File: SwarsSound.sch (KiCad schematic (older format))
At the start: 9 parts, among them P1 Main_Connector

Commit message: Add files via upload
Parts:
- added 5F/H, F/H-5: 74LS125, symbol 74xx:74LS125
- added C1, C12, C61, C8, C9: 0.1uf, symbol Device:C
- added H-5: LS74, symbol Star_Wars_Vector_PCB:LS74
- added R1: 1000, symbol Device:R_US
- added R2, R3: 10K, symbol Device:R_US
- F_5: symbol Star_Wars_Audio_PCB:LS161A -> SwarsSound-rescue:LS161A-Star_Wars_Audio_PCB
- gave numbers to parts that had none: 3
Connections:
- net labels added: MAINFLAG, P, SA0, SA1, SA10, SA11, SA12, SA13, SA14, SA2, SA3, SA4, SA5, SA6, SA7, SA8, SA9, SD0, SD1, SD2, SD3, SD4, SD5, SD6, SD7, SOUNDFLAG, SR\~W, S~IRQ, ~SOUNDREAD, ~SOUNDWR, ~SRES, ɸE
- wire segments 143 -> 197
- no-connect marks 43 -> 51
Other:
- note added: "Microprocessor"
- note added: "Parallel Interface with Full Handshaking"
- moved on the sheet: C6, H_2E, J_3B, J_5, K-3, K_5, R4

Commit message: Add files via upload
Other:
- note added: "Interface Flag Reader"
- moved on the sheet: 5F/HB, 5F/HC
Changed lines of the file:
@@
 L 74xx:74LS125 5F/H
 U 3 1 60E16230
-P 13400 8250
-F 0 "5F/H" H 13400 8567 50  0000 C CNN
-F 1 "74LS125" H 13400 8476 50  0000 C CNN
-F 2 "" H 13400 8250 50  0001 C CNN
-F 3 "http://www.ti.com/lit/gpn/sn74LS125" H 13400 8250 50  0001 C CNN
-	3    13400 8250
+P 13675 8400
+F 0 "5F/H" H 13675 8717 50  0000 C CNN
+F 1 "74LS125" H 13675 8626 50  0000 C CNN
+F 2 "" H 13675 8400 50  0001 C CNN
+F 3 "http://www.ti.com/lit/gpn/sn74LS125" H 13675 8400 50  0001 C CNN
+	3    13675 8400
 	1    0    0    -1
 $EndComp
@@
 L 74xx:74LS125 5F/H
 U 2 1 60E1786D
-P 13400 9150
-F 0 "5F/H" H 13400 9467 50  0000 C CNN
-F 1 "74LS125" H 13400 9376 50  0000 C CNN
-F 2 "" H 13400 9150 50  0001 C CNN
-F 3 "http://www.ti.com/lit/gpn/sn74LS125" H 13400 9150 50  0001 C CNN
-	2    13400 9150
+P 13675 9300
+F 0 "5F/H" H 13675 9617 50  0000 C CNN
+F 1 "74LS125" H 13675 9526 50  0000 C CNN
+F 2 "" H 13675 9300 50  0001 C CNN
+F 3 "http://www.ti.com/lit/gpn/sn74LS125" H 13675 9300 50  0001 C CNN
+	2    13675 9300
 	1    0    0    -1
 $EndComp
-Text GLabel 13100 8250 0    60   Input ~ 0
+Text GLabel 13375 8400 0    60   Input ~ 0
 MAINFLAG
-Text GLabel 13100 9150 0    60   Input ~ 0
+Text GLabel 13375 9300 0    60   Input ~ 0
 SOUNDFLAG
 Wire Wire Line
-	13350 9150 13100 9150
-Text GLabel 13700 8250 2    60   Input ~ 0
+	13625 9300 13375 9300
+Text GLabel 13975 8400 2    60   Input ~ 0
 PD7
 Wire Wire Line
-	13400 8500 13400 8650
+	13675 8650 13675 8800
 Wire Wire Line
-	13400 8650 12375 8650
-Text GLabel 12150 8650 0    60   Input ~ 0
+	13675 8800 12650 8800
+Text GLabel 12425 8800 0    60   Input ~ 0
 ~FLAGREAD
 Wire Wire Line
-	12375 8650 12375 9625
+	12650 8800 12650 9775
 Wire Wire Line
-	12375 9625 13400 9625
+	12650 9775 13675 9775
 Wire Wire Line
-	13400 9625 13400 9400
-Connection ~ 12375 8650
+	13675 9775 13675 9550
+Connection ~ 12650 8800
 Wire Wire Line
-	12375 8650 12150 8650
-Text GLabel 13700 9150 2    60   Input ~ 0
+	12650 8800 12425 8800
+Text GLabel 13975 9300 2    60   Input ~ 0
 PD6
 Wire Notes Line width 40 style solid rgb(0, 0, 0)
@@
 Wire Notes Line width 40 style solid rgb(0, 0, 0)
 	11225 9975 11225 7500
+Text Notes 14000 7775 2    100  ~ 20
+Interface Flag Reader
 $EndSCHEMATC

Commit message: Joint session
Added footprints and plopped chips on nonexistent board.
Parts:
- removed 5F/H: 74LS125, symbol 74xx:74LS125
- removed F_5: LS161A, symbol SwarsSound-rescue:LS161A-Star_Wars_Audio_PCB
- added A-3: NE556, Star_Wars_Vector_PCB:DIP14, symbol SwarsSound-rescue:NE556-Timer
- added B-2, C-3, C-4: TL084, Star_Wars_Vector_PCB:DIP14, symbol SwarsSound-rescue:TL084-Amplifier_Operational
- added B-3: RD5106A, Star_Wars_Vector_PCB:DIP8, symbol SwarsSound-rescue:RD5106A-Audio
- added C/D-1: TMS-5220, Star_Wars_Main_PCB:DIP28, symbol Star_Wars_Audio_PCB:TMS-5220
- added C10, C11, C16, C17, C18, C19, C2, C20, C28, C3, C4, C5, C7: 0.1uf, Star_Wars_Vector_PCB:GenericComp, symbol Device:C
- added C22, C23, C24, C25, C26, C27, C30, C31, C32, C34, C36, C37, C38, C40, C41, C42, C43, C45, C54, C55, C59, C60: 0.1, Star_Wars_Vector_PCB:GenericComp, symbol Device:C
- added C29, C33, C35, C39: 1000pf, Star_Wars_Vector_PCB:GenericComp, symbol Device:C
- added C44: 0.01, Star_Wars_Vector_PCB:GenericComp, symbol Device:C
- added C46, C48, C49, C50, C56, C57, C58: .0027, Star_Wars_Vector_PCB:GenericComp, symbol Device:C
- added C47, C53: 100, Star_Wars_Vector_PCB:GenericComp, symbol Device:C
- added C51: 0.47, Star_Wars_Vector_PCB:GenericComp, symbol Device:C
- added C52: 10, Star_Wars_Vector_PCB:GenericComp, symbol Device:C
- added D-2: CI/O 3, Package_DIP:DIP-40_W15.24mm, symbol SwarsSound-rescue:POKEY-Star_Wars_Audio_PCB
- added D-3: CI/O 2, Package_DIP:DIP-40_W15.24mm, symbol SwarsSound-rescue:POKEY-Star_Wars_Audio_PCB
- added D-4: CI/O 1, Package_DIP:DIP-40_W15.24mm, symbol SwarsSound-rescue:POKEY-Star_Wars_Audio_PCB
- added D-5: CI/O 0, Package_DIP:DIP-40_W15.24mm, symbol SwarsSound-rescue:POKEY-Star_Wars_Audio_PCB
- added E-1: 6532A PIA, Package_DIP:DIP-40_W15.24mm, symbol SwarsSound-rescue:6532A-Star_Wars_Audio_PCB
- added F-2: CD4069/74C04, Star_Wars_Vector_PCB:DIP14, symbol SwarsSound-rescue:4069-4xxx
- added F-3, F-5: LS161A, Star_Wars_Vector_PCB:DIP16, symbol Star_Wars_Audio_PCB:LS161A
- added F/H-1: 6116-2K-RAM, Star_Wars_Vector_PCB:DDIP24, symbol SwarsSound-rescue:6116-2K-RAM
- added unit 3 of F/H-5
- added unit 2 of F/H-5
- added H-1, J/K-1: 2764, Star_Wars_Main_PCB:DIP28, symbol star_wars_arcade_main_pcb:2764
- added H-2: LS04, Star_Wars_Vector_PCB:DIP14, symbol Star_Wars_Vector_PCB:LS04
- added H-3: LS00, Star_Wars_Vector_PCB:DIP14, symbol Asteroids:LS00
- added J-2: LS139, Star_Wars_Vector_PCB:DIP16, symbol Asteroids:LS139
- added unit 1 of J-3
- added P2: aud_con, Star_Wars_Vector_PCB:Aud_Con_7, symbol Star_Wars_Audio_PCB:aud_con
- added P3: edge_con, Star_Wars_Vector_PCB:J20, symbol Star_Wars_Audio_PCB:edge_con
- added Q1, Q2: 2N3906f, Star_Wars_Vector_PCB:GenericTrans, symbol SwarsSound-rescue:2N3906f-Transistor_BJT
- added Q3, Q4: 2N3904, Package_TO_SOT_THT:TO-92_Inline, symbol Transistor_BJT:2N3904
- added R10, R13, R17, R37, R5, R6: 10K, Star_Wars_Vector_PCB:GenericComp, symbol Device:R_US
- added R11, R14, R16: 3300, Star_Wars_Vector_PCB:GenericComp, symbol Device:R_US
- added R12, R15, R20, R22, R24, R26, R28: 1000, Star_Wars_Vector_PCB:GenericComp, symbol Device:R_US
- added R18: 1800, Star_Wars_Vector_PCB:GenericComp, symbol Device:R_US
- added R19: 100K, Star_Wars_Vector_PCB:GenericComp, symbol Device:R_US
- added R21, R23, R50, R54, R55: 47K, Star_Wars_Vector_PCB:GenericComp, symbol Device:R_US
- added R25, R27: 82K, Star_Wars_Vector_PCB:GenericComp, symbol Device:R_US
- added R29: 15K, Star_Wars_Vector_PCB:GenericComp, symbol Device:R_US
- added R30, R39, R40, R42, R46, R47: 12K, Star_Wars_Vector_PCB:GenericComp, symbol Device:R_US
- added R31, R32: 560K, Star_Wars_Vector_PCB:GenericComp, symbol Device:R_US
- added R33, R34: 4700, Star_Wars_Vector_PCB:GenericComp, symbol Device:R_US
- added R35, R51, R56: 2.2K, Star_Wars_Vector_PCB:GenericComp, symbol Device:R_US
- added R36: 15, Star_Wars_Vector_PCB:GenericComp, symbol Device:R_US
- added R38: 470, Star_Wars_Vector_PCB:GenericComp, symbol Device:R_US
- added R41: 68K, Star_Wars_Vector_PCB:GenericComp, symbol Device:R_US
- added R43: 1500, Star_Wars_Vector_PCB:GenericComp, symbol Device:R_US
- added R44, R8, R9: 100, Star_Wars_Vector_PCB:GenericComp, symbol Device:R_US
- added R45: 470K, Star_Wars_Vector_PCB:GenericComp, symbol Device:R_US
- added R48, R49, R52, R53: 22K, Star_Wars_Vector_PCB:GenericComp, symbol Device:R_US
- added TP1, TP10, TP2, TP7, TP8, TP9: TP, Star_Wars_Vector_PCB:TEST_POINT, symbol Star_Wars_Vector_PCB:TP
- C1, C12, C6, C61, C8, C9, R1, R2, R3, R4: footprint (none) -> Star_Wars_Vector_PCB:GenericComp
- F/H-5, H-5, H_2: footprint (none) -> Star_Wars_Vector_PCB:DIP14
- J-3: renamed from J_3; footprint (none) -> Star_Wars_Vector_PCB:DIP16
- J-5: renamed from J_5; footprint (none) -> Star_Wars_Vector_PCB:DIP20
- K-3: footprint (none) -> Star_Wars_Vector_PCB:DDIP40
- K-5: renamed from K_5; footprint (none) -> Star_Wars_Vector_PCB:DIP20
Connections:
- net labels added: +12V, +5A, -5V, AUD, CO0, CO1, CO2, CO3, DRCV, DXMT, LT_AUD, PA0, PA1, PA2, PA3, PA5, PB0, PB1, PB2, PB3, PB4, PB5, PB6, PB7, RCK, RT_AUD, SPEECH, SUM, ~CI\O, ~CI\O0, ~CI\O1, ~CI\O2, ~CI\O3, ~PIA, ~SRAM, ~SROM0, ~SROM1
- wire segments 197 -> 497
- no-connect marks 51 -> 101
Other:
- note added: "Address Decoders"
- note added: "Buffers"
- note added: "Delay"
- note added: "Delay Clock"
- note added: "Filter"
- note added: "Music and Sound Effects Generators"
- note added: "Not fitted"
- note added: "Output and Summing Amplifiers"
- note added: "Peripheral Interface Adapter"
- note added: "SELF-TEST"
- note added: "Sound RAM\n"
- note added: "Sound ROM"
- note added: "Speech Synthesizer"
- note added: "Speech Synthesizer Clock Generator"
- note added: "Speech Synthesizer Power Switch"
- note added: "Summing Amplifier"
- note added: "Used by buffers"
- moved on the sheet: C1, C6, C8, C9, F/H-5E, H-5B, J-3B, J-5, K-5

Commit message: Began board layout
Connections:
- net +12V: now also A-3.14 (VCC)
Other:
- moved on the sheet: C45
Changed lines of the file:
@@
 $EndComp
 NoConn ~ 22575 14550
-Wire Wire Line
-	22375 14150 22225 14150
-Wire Wire Line
-	22225 13925 22225 14100
 $Comp
 L power:GND #PWR0130
 U 1 1 61A178FF
-P 22675 14150
-F 0 "#PWR0130" H 22675 13900 50  0001 C CNN
-F 1 "GND" H 22680 13977 50  0000 C CNN
-F 2 "" H 22675 14150 50  0001 C CNN
-F 3 "" H 22675 14150 50  0001 C CNN
-	1    22675 14150
+P 22775 14100
+F 0 "#PWR0130" H 22775 13850 50  0001 C CNN
+F 1 "GND" H 22780 13927 50  0000 C CNN
+F 2 "" H 22775 14100 50  0001 C CNN
+F 3 "" H 22775 14100 50  0001 C CNN
+	1    22775 14100
 	1    0    0    -1
 $EndComp
-Connection ~ 22225 14100
 $Comp
 L Device:C C45
 U 1 1 619FBD8D
-P 22525 14150
-F 0 "C45" V 22725 14150 50  0000 C CNN
-F 1 "0.1" V 22650 14150 50  0000 C CNN
-F 2 "Star_Wars_Vector_PCB:GenericComp" H 22563 14000 50  0001 C CNN
-F 3 "~" H 22525 14150 50  0001 C CNN
-	1    22525 14150
+P 22625 14100
+F 0 "C45" V 22825 14100 50  0000 C CNN
+F 1 "0.1" V 22750 14100 50  0000 C CNN
+F 2 "Star_Wars_Vector_PCB:GenericComp" H 22663 13950 50  0001 C CNN
+F 3 "~" H 22625 14100 50  0001 C CNN
+	1    22625 14100
 	0    -1   -1   0
 $EndComp
 Connection ~ 21925 14100
 Wire Wire Line
-	22225 14100 22225 14150
-Wire Wire Line
-	21925 14100 22225 14100
+	21925 14100 22250 14100
 Wire Wire Line
 	21925 14100 21925 14150
 Wire Wire Line
 	21050 14100 21925 14100
-Connection ~ 21575 14700
 Wire Wire Line
 	21575 14550 21575 14700
@@
 	1    0    0    -1
 $EndComp
-$Comp
-L SwarsSound-rescue:NE556-Timer A-3
-U 1 1 618D148D
-P 22075 14550
-F 0 "A-3" H 22125 14600 50  0000 R CNN
-F 1 "NE556" H 22150 14500 50  0000 R CNN
-F 2 "Star_Wars_Vector_PCB:DIP14" H 22075 14550 50  0001 C CNN
-F 3 "http://www.ti.com/lit/ds/symlink/ne556.pdf" H 22075 14550 50  0001 C CNN
-	1    22075 14550
-	1    0    0    -1
-$EndComp
 Wire Wire Line
 	22450 15425 22450 15250
@@
 L power:+12V #PWR0236
 U 1 1 61EDFE84
-P 22225 13925
-F 0 "#PWR0236" H 22225 13775 50  0001 C CNN
-F 1 "+12V" H 22240 14098 50  0000 C CNN
-F 2 "" H 22225 13925 50  0001 C CNN
-F 3 "" H 22225 13925 50  0001 C CNN
-	1    22225 13925
+P 22250 13925
+F 0 "#PWR0236" H 22250 13775 50  0001 C CNN
+F 1 "+12V" H 22265 14098 50  0000 C CNN
+F 2 "" H 22250 13925 50  0001 C CNN
+F 3 "" H 22250 13925 50  0001 C CNN
+	1    22250 13925
 	1    0    0    -1
 $EndComp
@@
 	1    0    0    -1
 $EndComp
+Connection ~ 21575 14700
+$Comp
+L SwarsSound-rescue:NE556-Timer A-3
+U 1 1 618D148D
+P 22075 14550
+F 0 "A-3" H 22125 14600 50  0000 R CNN
+F 1 "NE556" H 22150 14500 50  0000 R CNN
+F 2 "Star_Wars_Vector_PCB:DIP14" H 22075 14550 50  0001 C CNN
+F 3 "http://www.ti.com/lit/ds/symlink/ne556.pdf" H 22075 14550 50  0001 C CNN
+	1    22075 14550
+	1    0    0    -1
+$EndComp
+Wire Wire Line
+	22250 13925 22250 14100
+Wire Wire Line
+	22250 14100 22475 14100
+Connection ~ 22250 14100
+Wire Wire Line
+	22250 14150 22250 14100
 $EndSCHEMATC

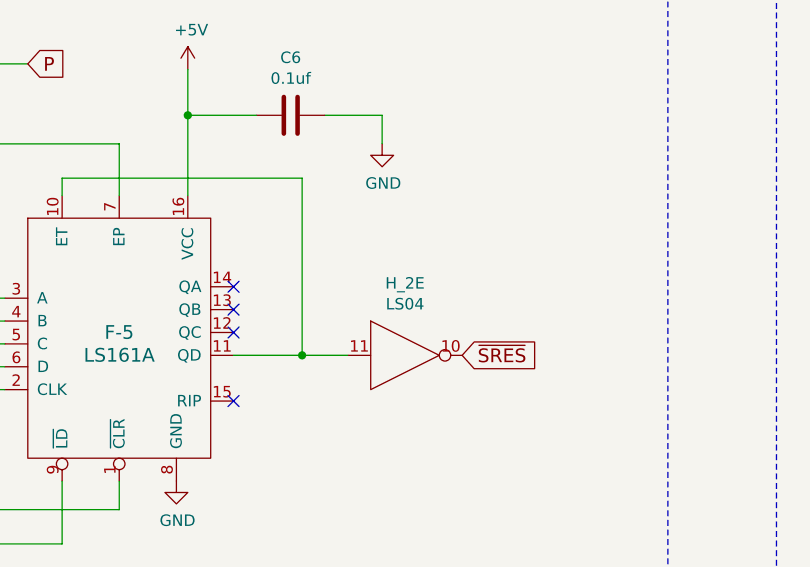
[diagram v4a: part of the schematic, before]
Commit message: Finished chip layout
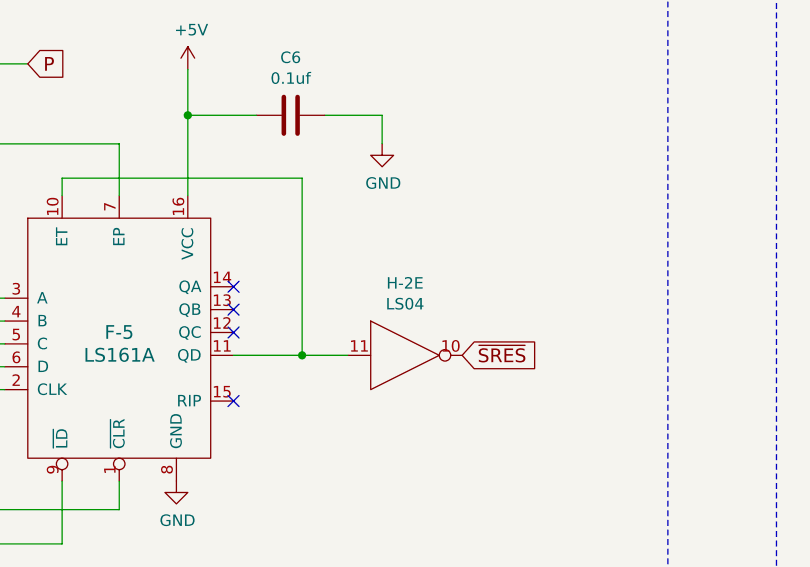
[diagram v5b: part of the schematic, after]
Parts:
- renumbered H_2 to H-2
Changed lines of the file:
@@
 $EndComp
 $Comp
-L Star_Wars_Vector_PCB:LS04 H_2
+L Star_Wars_Vector_PCB:LS04 H-2
 U 5 1 60E01303
 P 4325 3300
-F 0 "H_2" H 4325 3615 50  0000 C CNN
+F 0 "H-2" H 4325 3615 50  0000 C CNN
 F 1 "LS04" H 4325 3524 50  0000 C CNN
 F 2 "Star_Wars_Vector_PCB:DIP14" H 4325 3300 50  0001 C CNN

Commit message: next push
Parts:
- added TP11: TP, Star_Wars_Vector_PCB:TEST_POINT, symbol Star_Wars_Vector_PCB:TP
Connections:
- net GND: now also TP11.1, TP11.2
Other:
- note added: "GND"
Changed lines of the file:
@@
 Wire Wire Line
 	22250 14150 22250 14100
+Text Notes 28450 1700 0    50   Italic 0
+GND
+$Comp
+L Star_Wars_Vector_PCB:TP TP11
+U 1 1 60E35091
+P 28650 1925
+F 0 "TP11" H 28769 1917 60  0000 L CNN
+F 1 "TP" H 28575 1975 60  0001 C CNN
+F 2 "Star_Wars_Vector_PCB:TEST_POINT" H 28575 1875 60  0001 C CNN
+F 3 "" H 28575 1875 60  0001 C CNN
+	1    28650 1925
+	1    0    0    -1
+$EndComp
+Wire Wire Line
+	27675 1950 28575 1950
+Wire Wire Line
+	28575 1950 28575 2125
+Connection ~ 27675 1950
+Wire Wire Line
+	28725 2125 28575 2125
+Connection ~ 28575 2125
 $EndSCHEMATC

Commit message: Added TPs and large caps
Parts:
- added C13, C14, C15: 100, Star_Wars_Vector_PCB:LargeCap, symbol Device:C
- added DS1: LED, Star_Wars_Vector_PCB:LED, symbol Device:LED
- added R7: 150, Star_Wars_Vector_PCB:GenericComp, symbol Device:R_US
- added TP12, TP3, TP4, TP5, TP6: TP, Star_Wars_Vector_PCB:TEST_POINT, symbol Star_Wars_Vector_PCB:TP
- C47, C53: footprint Star_Wars_Vector_PCB:GenericComp -> Star_Wars_Vector_PCB:LargeCap
- C51, C52: footprint Star_Wars_Vector_PCB:GenericComp -> Star_Wars_Main_PCB:Cap1
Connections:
- net +12V: now also C13.2, TP5.1, TP5.2
- net +5V: now also C15.2, R7.1, TP6.1, TP6.2
- net -5V: now also C14.2, TP4.1, TP4.2
- net GND: now also C13.1, C14.1, C15.1, DS1.1 (K), TP12.1, TP12.2, TP3.1, TP3.2
- new net: DS1.2 (A), R7.2
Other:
- note removed: "GND"
- moved on the sheet: P3, R51, R56, TP10, TP7, TP9

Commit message: fixes
fixed RAM (pin '28' -> 24) and finished RAM/ROM data bus.
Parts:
- F/H-1: symbol SwarsSound-rescue:6116-2K-RAM -> SwarsSound-rescue:6116-2K-RAM-SwarsSound-rescue
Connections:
- net +5V: now also F/H-1.24 (VCC); no longer F/H-1.28 (VCC)
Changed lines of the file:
@@
 Connection ~ 27150 1950
 $Comp
-L SwarsSound-rescue:6116-2K-RAM F/H-1
+L SwarsSound-rescue:6116-2K-RAM-SwarsSound-rescue F/H-1
 U 1 1 6158ABEB
 P 23725 7125
